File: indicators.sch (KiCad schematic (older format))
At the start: 4 parts

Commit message: Netlist and PCB generated
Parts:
- D1, D2: renamed from D?; footprint (none) -> LEDs:LED_0805
- R10, R11: renamed from R?; footprint (none) -> Resistors_SMD:R_0805_HandSoldering
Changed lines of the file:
@@
 $EndDescr
 $Comp
-L +5V #PWR?
+L +5V #PWR018
 U 1 1 57FDEE5C
 P 1000 750
-F 0 "#PWR?" H 1000 600 50  0001 C CNN
+F 0 "#PWR018" H 1000 600 50  0001 C CNN
 F 1 "+5V" H 1000 890 50  0000 C CNN
 F 2 "" H 1000 750 50  0000 C CNN
@@
 $EndComp
 $Comp
-L GND #PWR?
+L GND #PWR019
 U 1 1 57FDEE70
 P 1000 1650
-F 0 "#PWR?" H 1000 1400 50  0001 C CNN
+F 0 "#PWR019" H 1000 1400 50  0001 C CNN
 F 1 "GND" H 1000 1500 50  0000 C CNN
 F 2 "" H 1000 1650 50  0000 C CNN
@@
 $EndComp
 $Comp
-L R_Small R?
+L R_Small R10
 U 1 1 57FDEE84
 P 1000 950
-F 0 "R?" H 1030 970 50  0000 L CNN
+F 0 "R10" H 1030 970 50  0000 L CNN
 F 1 "150" H 1030 910 50  0000 L CNN
-F 2 "" H 1000 950 50  0000 C CNN
+F 2 "Resistors_SMD:R_0805_HandSoldering" H 1000 950 50  0001 C CNN
 F 3 "" H 1000 950 50  0000 C CNN
 	1    1000 950
@@
 	1000 850  1000 750
 $Comp
-L LED D?
+L LED D1
 U 1 1 57FDEF85
 P 1000 1350
-F 0 "D?" H 1000 1450 50  0000 C CNN
+F 0 "D1" H 1000 1450 50  0000 C CNN
 F 1 "POWER_LED" H 900 1200 50  0000 C CNN
-F 2 "" H 1000 1350 50  0000 C CNN
+F 2 "LEDs:LED_0805" H 1000 1350 50  0001 C CNN
 F 3 "" H 1000 1350 50  0000 C CNN
 	1    1000 1350
@@
 	1000 1650 1000 1550
 $Comp
-L +5V #PWR?
+L +5V #PWR020
 U 1 1 57FDF3E5
 P 1450 750
-F 0 "#PWR?" H 1450 600 50  0001 C CNN
+F 0 "#PWR020" H 1450 600 50  0001 C CNN
 F 1 "+5V" H 1450 890 50  0000 C CNN
 F 2 "" H 1450 750 50  0000 C CNN
@@
 $EndComp
 $Comp
-L GND #PWR?
+L GND #PWR021
 U 1 1 57FDF3EB
 P 1450 1650
-F 0 "#PWR?" H 1450 1400 50  0001 C CNN
+F 0 "#PWR021" H 1450 1400 50  0001 C CNN
 F 1 "GND" H 1450 1500 50  0000 C CNN
 F 2 "" H 1450 1650 50  0000 C CNN
@@
 $EndComp
 $Comp
-L R_Small R?
+L R_Small R11
 U 1 1 57FDF3F1
 P 1450 950
-F 0 "R?" H 1480 970 50  0000 L CNN
+F 0 "R11" H 1480 970 50  0000 L CNN
 F 1 "150" H 1480 910 50  0000 L CNN
-F 2 "" H 1450 950 50  0000 C CNN
+F 2 "Resistors_SMD:R_0805_HandSoldering" H 1450 950 50  0001 C CNN
 F 3 "" H 1450 950 50  0000 C CNN
 	1    1450 950
@@
 	1450 850  1450 750
 $Comp
-L LED D?
+L LED D2
 U 1 1 57FDF3F8
 P 1450 1350
-F 0 "D?" H 1450 1450 50  0000 C CNN
+F 0 "D2" H 1450 1450 50  0000 C CNN
 F 1 "SERVO_POWER_LED" H 1350 1200 50  0000 C CNN
-F 2 "" H 1450 1350 50  0000 C CNN
+F 2 "LEDs:LED_0805" H 1450 1350 50  0001 C CNN
 F 3 "" H 1450 1350 50  0000 C CNN
 	1    1450 1350

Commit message: PCB rev1.0
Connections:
- net +5V: no longer R11.1
- new net 5V_SERVO: R11.1
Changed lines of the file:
@@
 $EndDescr
 $Comp
-L +5V #PWR018
+L +5V #PWR015
 U 1 1 57FDEE5C
 P 1000 750
-F 0 "#PWR018" H 1000 600 50  0001 C CNN
+F 0 "#PWR015" H 1000 600 50  0001 C CNN
 F 1 "+5V" H 1000 890 50  0000 C CNN
 F 2 "" H 1000 750 50  0000 C CNN
@@
 $EndComp
 $Comp
-L GND #PWR019
+L GND #PWR016
 U 1 1 57FDEE70
 P 1000 1650
-F 0 "#PWR019" H 1000 1400 50  0001 C CNN
+F 0 "#PWR016" H 1000 1400 50  0001 C CNN
 F 1 "GND" H 1000 1500 50  0000 C CNN
 F 2 "" H 1000 1650 50  0000 C CNN
@@
 	1000 1650 1000 1550
 $Comp
-L +5V #PWR020
-U 1 1 57FDF3E5
-P 1450 750
-F 0 "#PWR020" H 1450 600 50  0001 C CNN
-F 1 "+5V" H 1450 890 50  0000 C CNN
-F 2 "" H 1450 750 50  0000 C CNN
-F 3 "" H 1450 750 50  0000 C CNN
-	1    1450 750
-	1    0    0    -1
-$EndComp
-$Comp
-L GND #PWR021
+L GND #PWR017
 U 1 1 57FDF3EB
 P 1450 1650
-F 0 "#PWR021" H 1450 1400 50  0001 C CNN
+F 0 "#PWR017" H 1450 1400 50  0001 C CNN
 F 1 "GND" H 1450 1500 50  0000 C CNN
 F 2 "" H 1450 1650 50  0000 C CNN
@@
 $EndComp
 Wire Wire Line
-	1450 850  1450 750
+	1450 625  1450 850
 $Comp
 L LED D2
@@
 Wire Wire Line
 	1450 1650 1450 1550
+Text GLabel 1525 625  2    60   Input ~ 0
+5V_SERVO
+Wire Wire Line
+	1450 625  1525 625
 $EndSCHEMATC

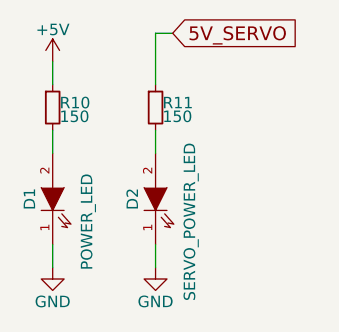
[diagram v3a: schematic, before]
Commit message: Jumper removed, pdf generated
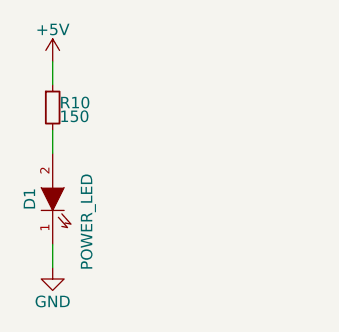
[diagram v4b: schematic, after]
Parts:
- removed D2: SERVO_POWER_LED, LEDs:LED_0805, symbol LED
- removed R11: 150, Resistors_SMD:R_0805_HandSoldering, symbol R_Small
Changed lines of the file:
@@
 $EndDescr
 $Comp
-L +5V #PWR015
+L +5V #PWR014
 U 1 1 57FDEE5C
 P 1000 750
-F 0 "#PWR015" H 1000 600 50  0001 C CNN
+F 0 "#PWR014" H 1000 600 50  0001 C CNN
 F 1 "+5V" H 1000 890 50  0000 C CNN
 F 2 "" H 1000 750 50  0000 C CNN
@@
 $EndComp
 $Comp
-L GND #PWR016
+L GND #PWR015
 U 1 1 57FDEE70
 P 1000 1650
-F 0 "#PWR016" H 1000 1400 50  0001 C CNN
+F 0 "#PWR015" H 1000 1400 50  0001 C CNN
 F 1 "GND" H 1000 1500 50  0000 C CNN
 F 2 "" H 1000 1650 50  0000 C CNN
@@
 Wire Wire Line
 	1000 1650 1000 1550
-$Comp
-L GND #PWR017
-U 1 1 57FDF3EB
-P 1450 1650
-F 0 "#PWR017" H 1450 1400 50  0001 C CNN
-F 1 "GND" H 1450 1500 50  0000 C CNN
-F 2 "" H 1450 1650 50  0000 C CNN
-F 3 "" H 1450 1650 50  0000 C CNN
-	1    1450 1650
-	1    0    0    -1
-$EndComp
-$Comp
-L R_Small R11
-U 1 1 57FDF3F1
-P 1450 950
-F 0 "R11" H 1480 970 50  0000 L CNN
-F 1 "150" H 1480 910 50  0000 L CNN
-F 2 "Resistors_SMD:R_0805_HandSoldering" H 1450 950 50  0001 C CNN
-F 3 "" H 1450 950 50  0000 C CNN
-	1    1450 950
-	1    0    0    -1
-$EndComp
-Wire Wire Line
-	1450 625  1450 850
-$Comp
-L LED D2
-U 1 1 57FDF3F8
-P 1450 1350
-F 0 "D2" H 1450 1450 50  0000 C CNN
-F 1 "SERVO_POWER_LED" H 1350 1200 50  0000 C CNN
-F 2 "LEDs:LED_0805" H 1450 1350 50  0001 C CNN
-F 3 "" H 1450 1350 50  0000 C CNN
-	1    1450 1350
-	0    -1   -1   0
-$EndComp
-Wire Wire Line
-	1450 1150 1450 1050
-Wire Wire Line
-	1450 1650 1450 1550
-Text GLabel 1525 625  2    60   Input ~ 0
-5V_SERVO
-Wire Wire Line
-	1450 625  1525 625
 $EndSCHEMATC
